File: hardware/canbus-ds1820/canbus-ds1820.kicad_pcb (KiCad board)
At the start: 4 copper layers, 55 x 35 mm, 34 parts, among them J1 USB_B_Micro, J2 UART, J3 10k NTC, J4 CANBus, J5 CANBus, J6 SWD, Q1 2N7002, Q2 2N7002, U1 MCP1754S-3302xCB, U2 STM32F042F6Px, U3 Voltage Regulator, U4 MCP2562HD

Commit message: Updated canbus-ds1820 board, reannotated canbus-gpios
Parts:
- removed the J3 at (103.3, 77.4)
- removed the R4 at (84.8, 75.9)
- removed R7: 10k, Resistor_SMD:R_0805_2012Metric_Pad1.20x1.40mm_HandSolder
- added J4: 3-pole terminal, TerminalBlock_TE-Connectivity:TerminalBlock_TE_282834-3_1x03_P2.54mm_Horizontal, F.Cu at (104.7, 75.3)
- added Q3: BSS84, Package_TO_SOT_SMD:SOT-23, B.Cu at (105.3, 85.7)
- added R6: 10k, Resistor_SMD:R_0805_2012Metric_Pad1.20x1.40mm_HandSolder, B.Cu at (106.8, 91.0)
- added U4: DS2482S-100+, UltraLibrarian:DS2482S-100&plus_, F.Cu at (104.1, 85.9)
- R3: value 499k 1% -> 10k
- moved R3 23.5 mm to (101.2, 86.5), turned to -90 degrees
- renumbered C2 to C1, C1 to C2, C5 to C3, C3 to C5, J6 to J2, J2 to J3, J4 to J5, J5 to J6, R5 to R4, R6 to R5, U4 to U5
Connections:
- R3 pad 1: +12V -> +3V3
- R3 pad 2: VBAT_MON -> SCL
- U2 pad 10: ~{SPI1_SS} -> unconnected-(U2-Pad10)
- U2 pad 11: SPI1_SCK -> unconnected-(U2-Pad11)
- U2 pad 12: SPI1_MISO -> unconnected-(U2-Pad12)
- U2 pad 13: SPI1_MOSI -> unconnected-(U2-Pad13)
- U2 pad 2: SDA1 -> SDA
- U2 pad 3: SCL1 -> SCL
- U2 pad 6: VTHERM -> unconnected-(U2-Pad6)
- U2 pad 7: VBAT_MON -> unconnected-(U2-Pad7)
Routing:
- net SDA: track 0.00 -> 27.3 mm, vias 0 -> 2
- net VTHERM: track 25.1 -> 0.00 mm, vias 1 -> 0
- net SCL: track 0.00 -> 19.4 mm, vias 0 -> 2
- net VBAT_MON: track 17.4 -> 0.00 mm, vias 2 -> 0
- net DQ: track 0.00 -> 11.8 mm, vias 0 -> 1
- net +3V3: track 22.3 -> 28.2 mm, vias 6 -> 8
- net GND: track 16.5 -> 20.6 mm, vias 5 -> 7
- net +12V: track 14.4 -> 10.4 mm
- net PCTLZ: track 0.00 -> 2.27 mm, vias 0 -> 1
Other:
- board text added: "CANBus DS1820"
- board text removed: "CANBus Thermistor"

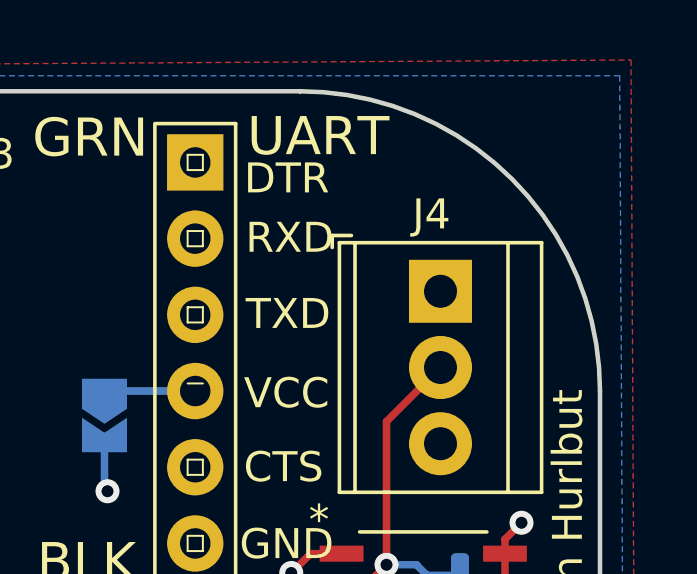
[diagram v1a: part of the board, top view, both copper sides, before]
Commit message: Updated the thermocouple board, added OSHW to bottom of all boards
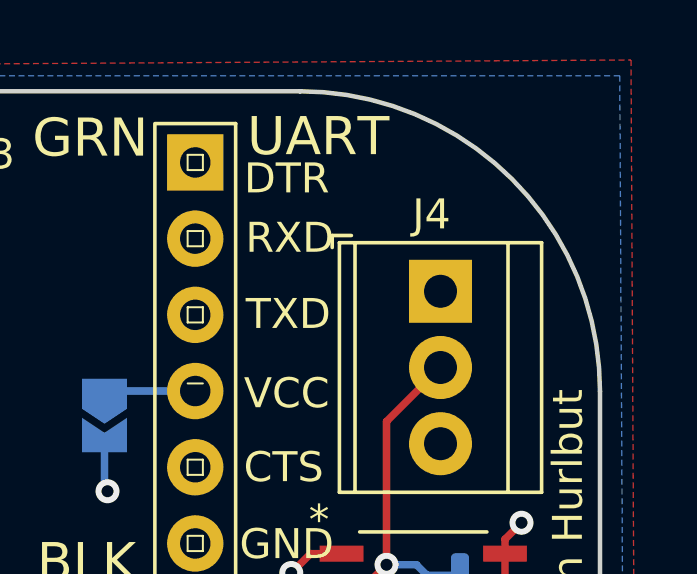
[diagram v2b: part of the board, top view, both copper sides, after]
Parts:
- added REF**: OSHW-Logo2_7.3x6mm_SilkScreen, Symbol:OSHW-Logo2_7.3x6mm_SilkScreen, B.Cu at (83.0, 76.0)
